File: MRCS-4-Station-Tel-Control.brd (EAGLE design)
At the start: 106 x 100 mm, 4 parts

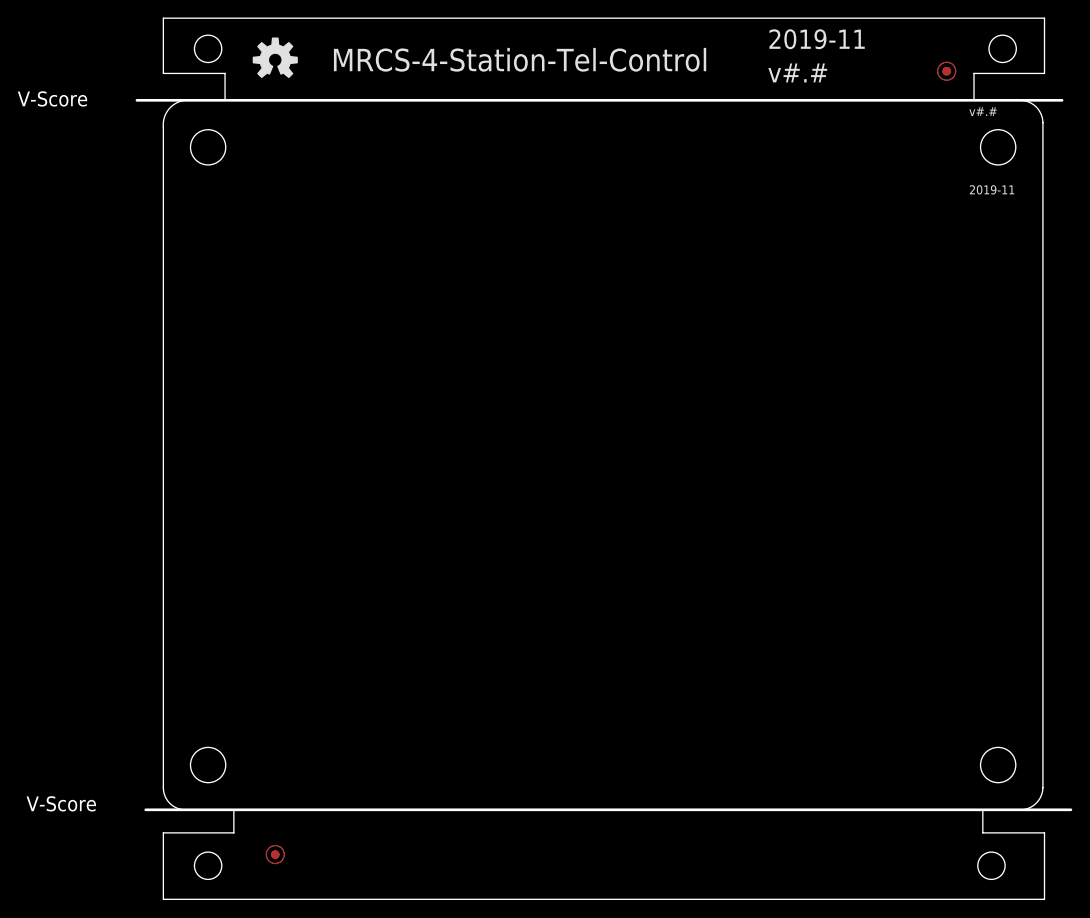
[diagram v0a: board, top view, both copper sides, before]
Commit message: First pass of board complete
This is the first iteration of the board.
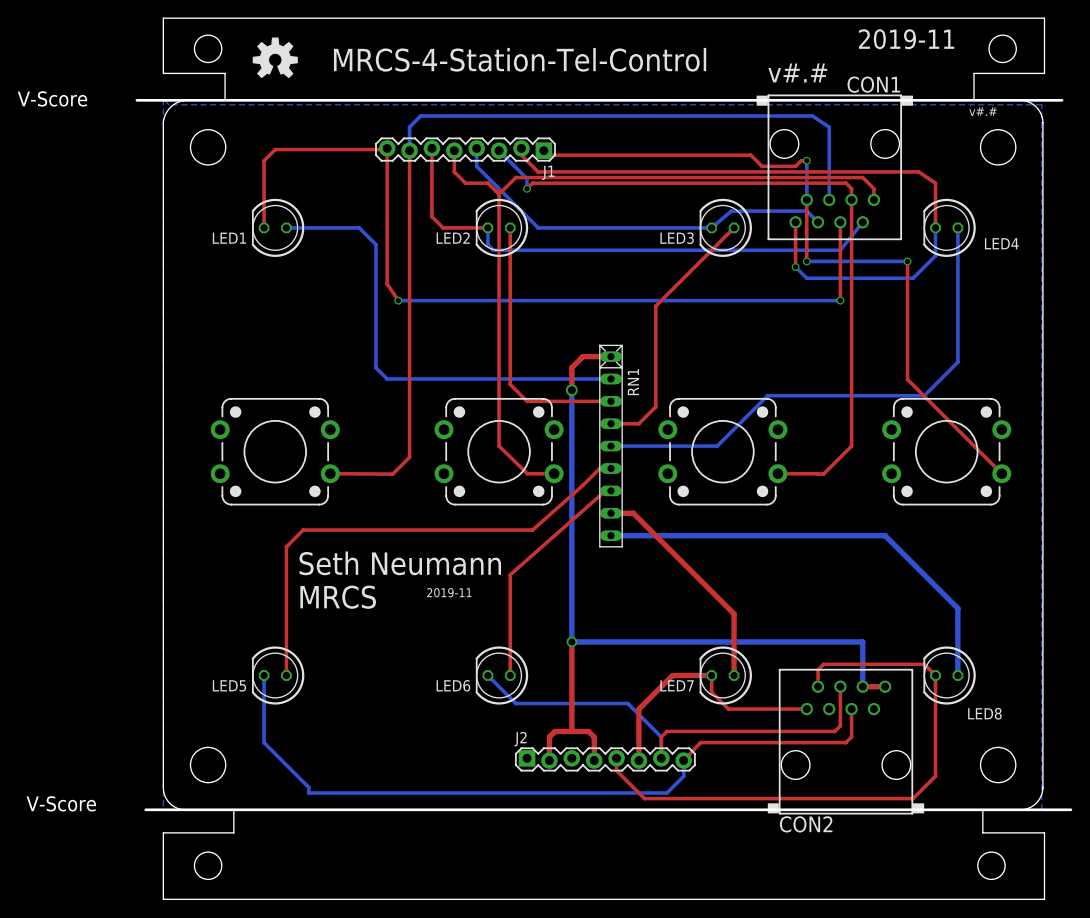
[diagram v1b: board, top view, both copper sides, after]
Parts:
- removed FID1, FID2: FIDUCIAL, SPCoast:FIDUCIAL_1MM
- added CON1: LEDs and Buttons RJ, SPCoast:RJ45-NO-SHIELD
- added CON2: LEDS & Pwr RJ, SPCoast:RJ45-NO-SHIELD
- added J1: LEDs & Buttons ST, SPCoast:1X08_LOCK
- added J2: LEDS & Pwr ST, SPCoast:1X08_LOCK
- added LED1, LED2, LED3, LED4, LED5, LED6, LED7, LED8: White, SPCoast:LED5MM
- added RN1: 4.7K, resistor-net:RN-9
- added S1, S2, S3, S4: SWITCH-MOMENTARY-212MM, SparkFun-Electromechanical:TACTILE-PTH-12MM
- added U$1: (no value), MRCSLogoTop:MRCSLOGOTOP
- added U$2: (no value), MRCS-prop65warningBtm:CA-PROP65WARNING
- added U$3: (no value), MRCSLogoBtm:MRCSLOGOBTM
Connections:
- new net +12V: CON2.6, CON2.8, J2.2, J2.4, RN1.1
- new net GND: CON2.3, CON2.7, J2.1, J2.3, S1.3, S2.3, S3.3, S4.3
- new net N$1: LED1.A, RN1.2
- new net N$12: CON1.1, J1.5, S2.1
- new net N$13: CON1.5, J1.7, S1.1
- new net N$14: CON1.3, J1.3, S3.1
- new net N$15: CON1.6, J1.4, LED3.K
- new net N$16: CON1.7, J1.1, S4.1
- new net N$17: CON1.8, J1.2, LED4.K
- new net N$18: CON1.2, J1.6, LED2.K
- new net N$2: LED2.A, RN1.3
- new net N$20: CON2.5, J2.8, LED5.K
- new net N$21: CON2.4, J2.7, LED6.K
- new net N$22: CON2.1, J2.6, LED7.K
- new net N$23: CON2.2, J2.5, LED8.K
- new net N$3: LED3.A, RN1.4
- new net N$4: LED4.A, RN1.5
- new net N$5: LED5.A, RN1.6
- new net N$6: LED6.A, RN1.7
- new net N$7: LED7.A, RN1.8
- new net N$8: LED8.A, RN1.9
- new net N$9: CON1.4, J1.8, LED1.K
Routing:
- net N$13: track 0.00 -> 104.0 mm
- net N$9: track 0.00 -> 98.7 mm, vias 0 -> 2
- net +12V: track 0.00 -> 97.8 mm, vias 0 -> 2
- net N$12: track 0.00 -> 90.0 mm
- net N$20: track 0.00 -> 83.9 mm
- net N$16: track 0.00 -> 82.2 mm, vias 0 -> 3
- net N$14: track 0.00 -> 81.9 mm, vias 0 -> 1
- net N$17: track 0.00 -> 79.7 mm, vias 0 -> 1
- net N$23: track 0.00 -> 67.4 mm
- net N$18: track 0.00 -> 60.9 mm
- net N$4: track 0.00 -> 58.6 mm
- net N$5: track 0.00 -> 54.9 mm
- net N$21: track 0.00 -> 52.7 mm
- net N$1: track 0.00 -> 52.1 mm
- net N$8: track 0.00 -> 50.4 mm
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- added copper zone on layer 16, net GND
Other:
- board text added: "Seth Neumann MRCS"
